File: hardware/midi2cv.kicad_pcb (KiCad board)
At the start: 2 copper layers, 20.3 x 128.5 mm, 83 parts, among them J1 MIDI In, J2 EuroPower10_THT, J3 Pitch, J4 Clock, J5 Clock2, J6 Gate, J7 MIDI Through, J8 CC, J9 Conn_02x04_Odd_Even, Q1 MMBT5551L, Q2 MMBT5551L, U1 EL3H7(C)(TA)-G, U3 TL072, U4 TL072

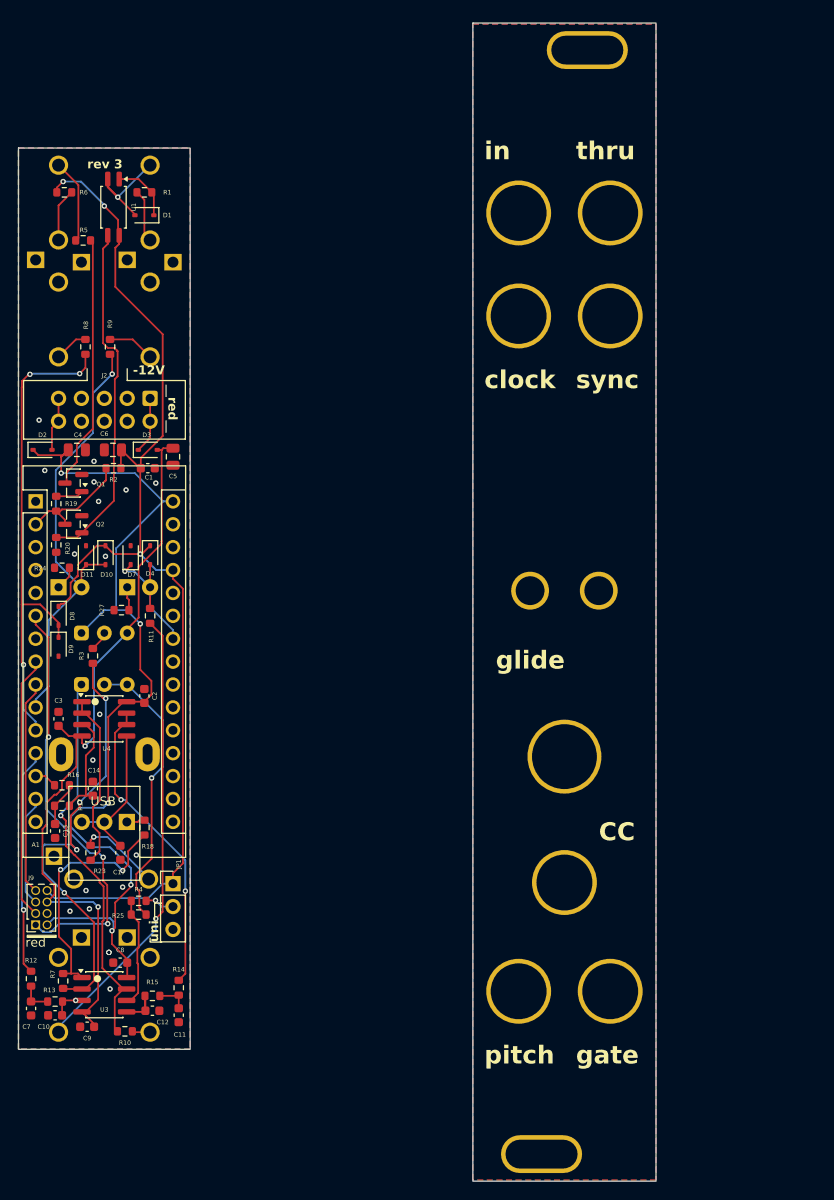
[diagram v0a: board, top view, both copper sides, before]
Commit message: main board rev 4: fix midi thru, led arrangement, glide cap value. fix sync trigger output
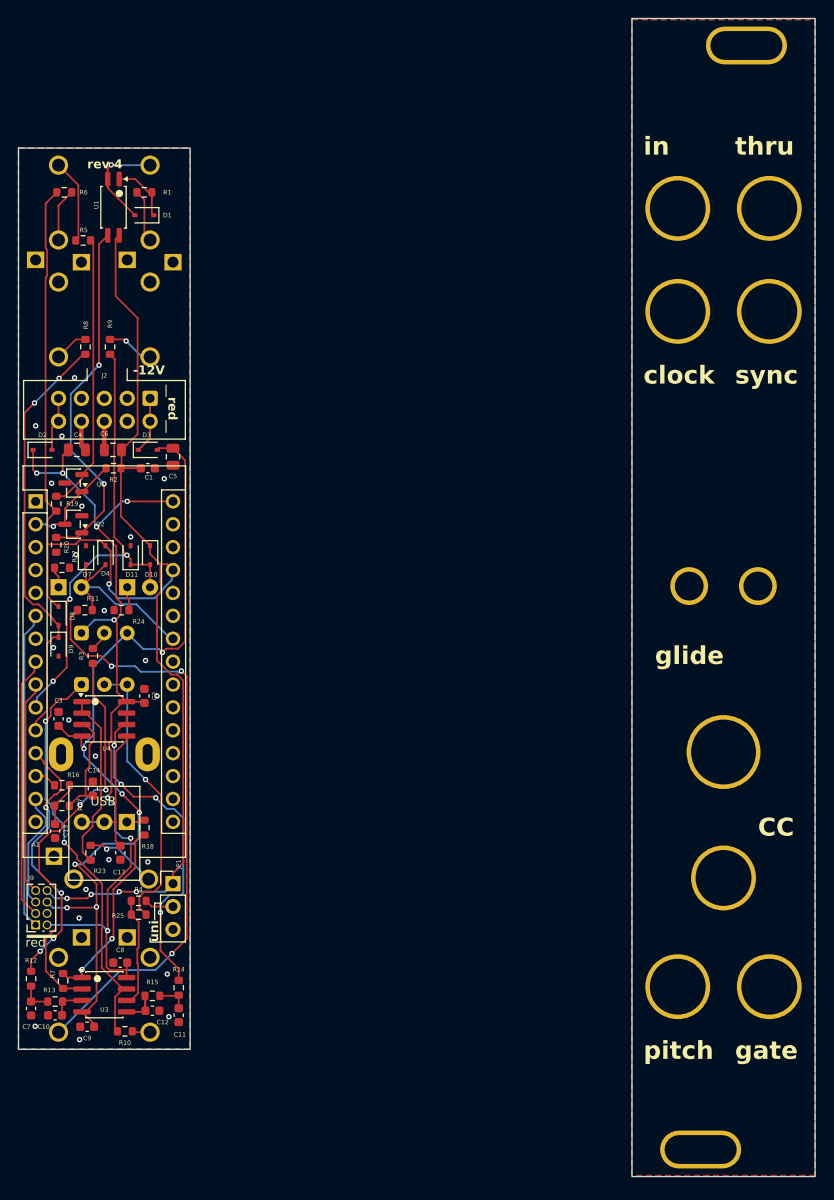
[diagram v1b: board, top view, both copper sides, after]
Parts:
- C17: value 10n -> 470n
- Q1: value MMBT5551L -> MMBT5401
- moved H1 17.7 mm to (190.6, 51.9)
- moved H2 17.7 mm to (190.6, 63.4)
- moved H4 17.7 mm to (190.6, 138.3)
- moved H5 17.7 mm to (200.8, 51.9)
- moved H6 17.7 mm to (200.8, 63.4)
- moved H7 17.7 mm to (200.8, 138.3)
- moved B3 17.7 mm to (195.7, 95.1)
- moved F 17.7 mm to (185.5, 34.2)
- moved H10 17.7 mm to (195.7, 112.3)
- moved H3 17.7 mm to (195.7, 126.2)
- moved H8 17.7 mm to (191.9, 93.9)
- moved H9 17.7 mm to (199.5, 93.9)
- moved R24 8.11 mm to (128.9, 96.5)
- moved R27 8.11 mm to (122.3, 91.8), turned to 0 degrees
- moved D5 7.62 mm to (129.5, 94.0)
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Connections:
- Q1 pad 1: Net-(Q1-B) -> MIDI_IN
- Q1 pad 2: B_GND -> Net-(Q1-E)
- Q1 pad 3: Net-(Q1-C) -> B_GND
- R19 pad 1: MIDI_IN -> Net-(Q1-E)
- R19 pad 2: Net-(Q1-B) -> B_+5V
- R5 pad 1: Net-(Q1-C) -> Net-(Q1-E)
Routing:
- net B_+5V: track 125.4 -> 166.0 mm, vias 3 -> 5
- net Net-(Q1-E): track 0.00 -> 30.8 mm
- net Net-(Q1-C): track 28.3 -> 0.00 mm
- net Net-(J6-PadT): track 50.7 -> 65.9 mm, vias 1 -> 3
- net B_-12V: track 84.1 -> 98.1 mm, vias 2 -> 7
- net EXP1: track 47.1 -> 35.3 mm, vias 3 -> 0
- net CLOCK: track 55.1 -> 48.0 mm, vias 3 -> 2
- net B_+12V: track 104.5 -> 97.8 mm, vias 5 -> 8
- net B_GND: track 0.00 -> 6.54 mm, vias 19 -> 22
- net GATE: track 16.1 -> 22.0 mm, vias 1 -> 0
- net SLEW_IN: track 27.0 -> 21.1 mm
- net PITCH: track 25.2 -> 30.0 mm, vias 1 -> 4
- net SLEW_OUT: track 34.2 -> 38.1 mm, vias 2 -> 4
- net Net-(U3A--): track 48.5 -> 45.2 mm, vias 4 -> 2
- net Net-(Q1-B): track 3.05 -> 0.00 mm
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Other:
- board text added: "rev 4"
- board text removed: "rev 3"
